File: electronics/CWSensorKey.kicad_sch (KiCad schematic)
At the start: 21 parts, among them J1 Tip, J2 GND, J3 Ring, J4 Dit, J5 Dah, J6 +, J7 -, Q1 IRFML8244TRPBF, Q2 IRFML8244TRPBF, U1 AT42QT1011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

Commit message: Branch (#3)
* index on main: b7a867d Further documentation in README.md Slightly changed dimensions of sensor pad Changed distance betw screws in sensor pad holder

* Adapted board for better fitting in the housing
Implemented script for generation of all 2D files from the KiCad models

* Delete electronics/gerbers directory

resolving merge conflict

* Update CWSensorKey.kicad_prl

updated active layer in kicad project file

---------

Co-authored-by: DL8ABG <dl8abg@qsl.net>
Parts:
- H1, H2, H3, H4: footprint MountingHole:MountingHole_2.7mm_M2.5_DIN965 -> MountingHole:MountingHole_3mm
- Q1, Q2: footprint Package_TO_SOT_SMD:SOT-23 -> Package_TO_SOT_SMD:SOT-23_Handsoldering
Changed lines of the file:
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@@
 			)
 		)
-		(property "Footprint" "MountingHole:MountingHole_2.7mm_M2.5_DIN965"
+		(property "Footprint" "MountingHole:MountingHole_3mm"
 			(at 138.43 130.81 0)
 			(effects
@@
 			)
 		)
-		(property "Footprint" "MountingHole:MountingHole_2.7mm_M2.5_DIN965"
+		(property "Footprint" "MountingHole:MountingHole_3mm"
 			(at 138.43 135.89 0)
 			(effects
@@
 			)
 		)
-		(property "Footprint" "MountingHole:MountingHole_2.7mm_M2.5_DIN965"
+		(property "Footprint" "MountingHole:MountingHole_3mm"
 			(at 138.43 140.97 0)
 			(effects
@@
 			)
 		)
-		(property "Footprint" "MountingHole:MountingHole_2.7mm_M2.5_DIN965"
+		(property "Footprint" "MountingHole:MountingHole_3mm"
 			(at 138.43 146.05 0)
 			(effects
@@
 			)
 		)
-		(property "Footprint" "Package_TO_SOT_SMD:SOT-23"
+		(property "Footprint" "Package_TO_SOT_SMD:SOT-23_Handsoldering"
 			(at 156.21 102.235 0)
 			(effects
@@
 			)
 		)
-		(property "Footprint" "Package_TO_SOT_SMD:SOT-23"
+		(property "Footprint" "Package_TO_SOT_SMD:SOT-23_Handsoldering"
 			(at 156.21 62.865 0)
 			(effects

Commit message: - Changed SMD resistors and capacitors to 1206 as this size is available within the kit from AATIS - Added picture of the board for better overview on github
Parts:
- C1, C2, C3, C4: footprint Capacitor_SMD:C_0805_2012Metric_Pad1.18x1.45mm_HandSolder -> Capacitor_SMD:C_1206_3216Metric_Pad1.33x1.80mm_HandSolder
- R1, R2: footprint Resistor_SMD:R_0805_2012Metric_Pad1.20x1.40mm_HandSolder -> Capacitor_SMD:C_1206_3216Metric_Pad1.33x1.80mm_HandSolder
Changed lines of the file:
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@@
 			)
 		)
-		(property "Footprint" "Resistor_SMD:R_0805_2012Metric_Pad1.20x1.40mm_HandSolder"
+		(property "Footprint" "Capacitor_SMD:C_1206_3216Metric_Pad1.33x1.80mm_HandSolder"
 			(at 102.87 56.642 90)
 			(effects
@@
 			)
 		)
-		(property "Footprint" "Resistor_SMD:R_0805_2012Metric_Pad1.20x1.40mm_HandSolder"
+		(property "Footprint" "Capacitor_SMD:C_1206_3216Metric_Pad1.33x1.80mm_HandSolder"
 			(at 102.87 96.012 90)
 			(effects
@@
 			)
 		)
-		(property "Footprint" "Capacitor_SMD:C_0805_2012Metric_Pad1.18x1.45mm_HandSolder"
+		(property "Footprint" "Capacitor_SMD:C_1206_3216Metric_Pad1.33x1.80mm_HandSolder"
 			(at 124.46 56.8452 0)
 			(effects
@@
 			)
 		)
-		(property "Footprint" "Capacitor_SMD:C_0805_2012Metric_Pad1.18x1.45mm_HandSolder"
+		(property "Footprint" "Capacitor_SMD:C_1206_3216Metric_Pad1.33x1.80mm_HandSolder"
 			(at 101.9048 69.85 0)
 			(effects
@@
 			)
 		)
-		(property "Footprint" "Capacitor_SMD:C_0805_2012Metric_Pad1.18x1.45mm_HandSolder"
+		(property "Footprint" "Capacitor_SMD:C_1206_3216Metric_Pad1.33x1.80mm_HandSolder"
 			(at 123.19 93.6752 0)
 			(effects
@@
 			)
 		)
-		(property "Footprint" "Capacitor_SMD:C_0805_2012Metric_Pad1.18x1.45mm_HandSolder"
+		(property "Footprint" "Capacitor_SMD:C_1206_3216Metric_Pad1.33x1.80mm_HandSolder"
 			(at 101.9048 109.22 0)
 			(effects

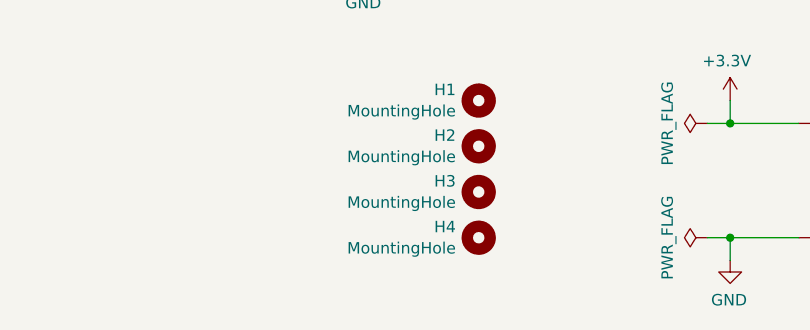
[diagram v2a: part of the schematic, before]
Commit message: - added option for mounting battery holder to board with screw - added information on AATIS kit number
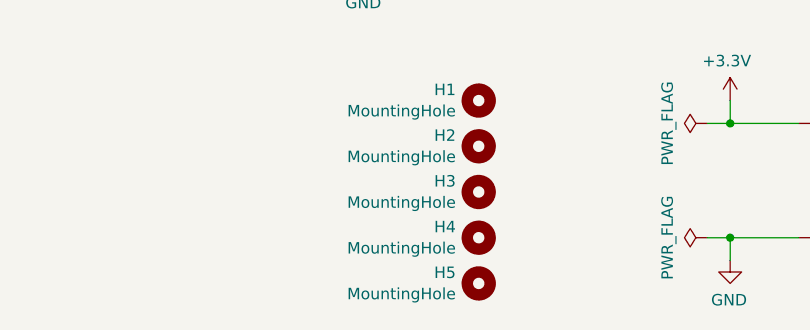
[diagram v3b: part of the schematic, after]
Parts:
- added H5: MountingHole, MountingHole:MountingHole_3mm, symbol Mechanical:MountingHole
- C1, C2, C3, C4: footprint Capacitor_SMD:C_1206_3216Metric_Pad1.33x1.80mm_HandSolder -> Capacitor_SMD:C_1210_3225Metric_Pad1.33x2.70mm_HandSolder
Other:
- company: DL8ABG in KiCad 9.0 (based on KM4NFQ) -> (none)
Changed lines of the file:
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@@
 		(date "2019-12-11")
 		(rev "1")
-		(company "DL8ABG in KiCad 9.0 (based on KM4NFQ)")
-		(comment 1 "2.2nF & 100nF CAPACITORS")
-		(comment 2 "22K OHM RESISTORS")
-		(comment 3 "IRFML8244TRPbF MOSFET")
-		(comment 4 "AT42QT1011 Touch Sensor")
+		(comment 1 "AATIS Kit No. AS686")
+		(comment 2 "DL8ABG in KiCad 9.0 (based on KM4NFQ)")
 	)
 	(text "GND"
@@
 			)
 		)
-		(property "Footprint" "Capacitor_SMD:C_1206_3216Metric_Pad1.33x1.80mm_HandSolder"
+		(property "Footprint" "Capacitor_SMD:C_1210_3225Metric_Pad1.33x2.70mm_HandSolder"
 			(at 124.46 56.8452 0)
 			(effects
@@
 			)
 		)
-		(property "Footprint" "Capacitor_SMD:C_1206_3216Metric_Pad1.33x1.80mm_HandSolder"
+		(property "Footprint" "Capacitor_SMD:C_1210_3225Metric_Pad1.33x2.70mm_HandSolder"
 			(at 101.9048 69.85 0)
 			(effects
@@
 			)
 		)
-		(property "Footprint" "Capacitor_SMD:C_1206_3216Metric_Pad1.33x1.80mm_HandSolder"
+		(property "Footprint" "Capacitor_SMD:C_1210_3225Metric_Pad1.33x2.70mm_HandSolder"
 			(at 123.19 93.6752 0)
 			(effects
@@
 			)
 		)
-		(property "Footprint" "Capacitor_SMD:C_1206_3216Metric_Pad1.33x1.80mm_HandSolder"
+		(property "Footprint" "Capacitor_SMD:C_1210_3225Metric_Pad1.33x2.70mm_HandSolder"
 			(at 101.9048 109.22 0)
 			(effects
@@
 					(unit 1)
 				)
+			)
+		)
+	)
+	(symbol
+		(lib_id "Mechanical:MountingHole")
+		(at 138.43 151.13 0)
+		(mirror y)
+		(unit 1)
+		(exclude_from_sim no)
+		(in_bom yes)
+		(on_board yes)
+		(dnp no)
+		(property "Reference" "H5"
+			(at 135.89 149.9362 0)
+			(effects
+				(font
+					(size 1.27 1.27)
+				)
+				(justify left)
+			)
+		)
+		(property "Value" "MountingHole"
+			(at 135.89 152.2984 0)
+			(effects
+				(font
+					(size 1.27 1.27)
+				)
+				(justify left)
+			)
+		)
+		(property "Footprint" "MountingHole:MountingHole_3mm"
+			(at 138.43 151.13 0)
+			(effects
+				(font
+					(size 1.27 1.27)
+				)
+				(hide yes)
+			)
+		)
+		(property "Datasheet" "~"
+			(at 138.43 151.13 0)
+			(effects
+				(font
+					(size 1.27 1.27)
+				)
+				(hide yes)
+			)
+		)
+		(property "Description" ""
+			(at 138.43 151.13 0)
+			(effects
+				(font
+					(size 1.27 1.27)
+				)
+				(hide yes)
+			)
+		)
+		(instances
+			(project "CWSensorKey"
+				(path "/246b0027-3286-4c16-89fc-199a4bf3d145"
+					(reference "H5")
+					(unit 1)
+				)
